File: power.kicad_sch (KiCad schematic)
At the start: 54 parts, among them J2 TYPE-C16PIN, J3 Conn_01x06_Pin, Q5 CSD17575Q3A, Q6 CSD17575Q3A, Q7 CSD17575Q3A, Q8 CSD17575Q3A, U1 FUSB302BMPX, U2 CH224K, U3 BQ25792RQMR, U4 AP2112K-3.3TRG1, U5 AP2112K-1.8TRG1, U6 LP8556SQ-E09/NOPB, U8 ESD7104MUTAG_C2987068, U9 TPS61088RHLR

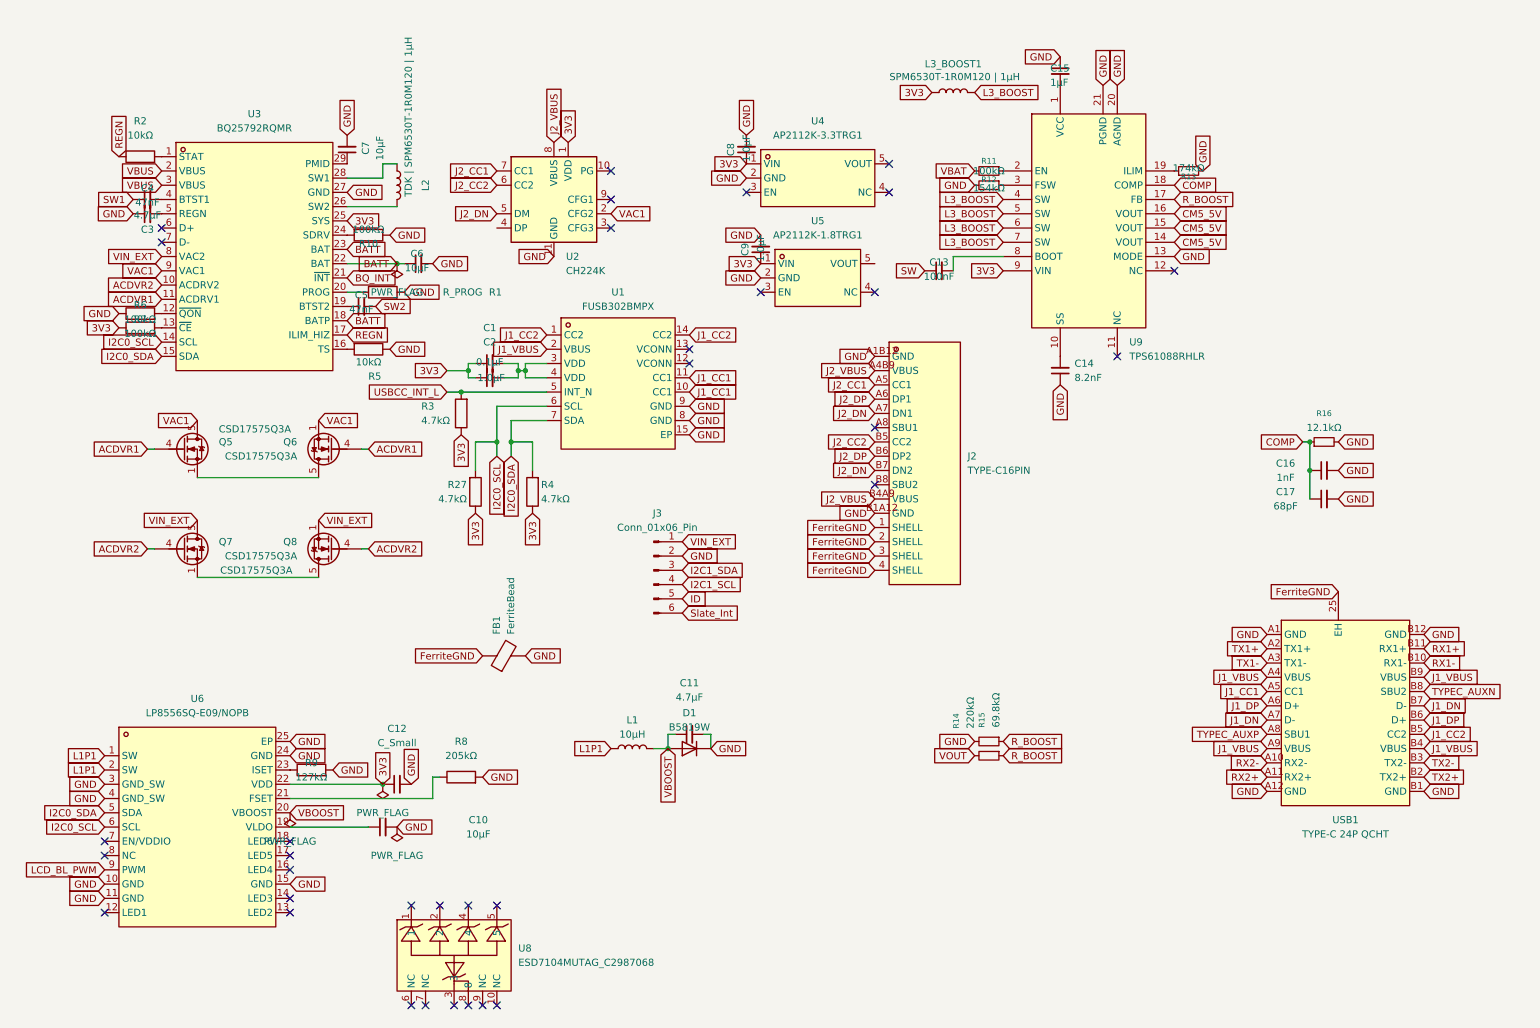
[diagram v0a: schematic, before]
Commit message: Move Data USB-C Port to IO + Add USB1 SS mux and SBU orientation switch, resolve CM5 GPIO assignments
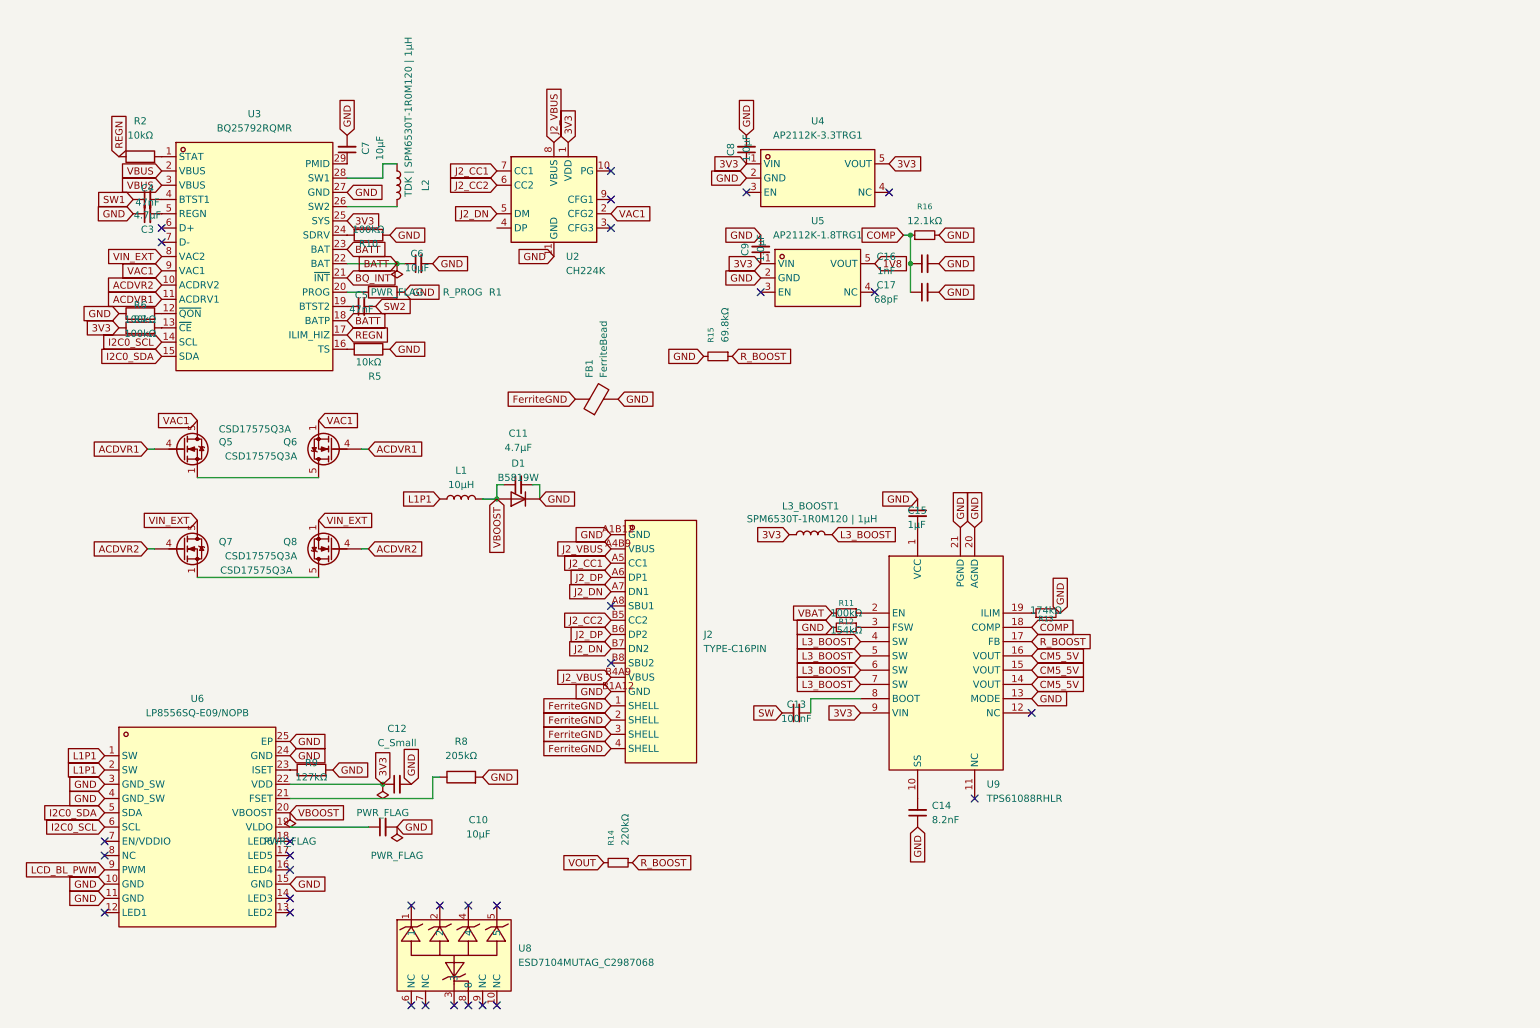
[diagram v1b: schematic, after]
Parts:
- removed C1: 0.1µF, symbol Device:C_Small
- removed C2: 1.0µF, symbol Device:C_Small
- removed J3: Conn_01x06_Pin, symbol Connector:Conn_01x06_Pin
- removed R27, R3, R4: 4.7kΩ, symbol Device:R
- removed U1: FUSB302BMPX, slate113:MLP-14_L2.5-W2.5-P0.50-BL-EP, symbol slate113:FUSB302BMPX
- removed USB1: TYPE-C 24P QCHT, slate113:TYPE-C-SMD_TYPE-C-24P-QCHT, symbol slate113:TYPE-C24PQCHT
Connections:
- net 3V3: now also U4.5 (VOUT)
- net 1V8: now reaches U5.5 (VOUT)
- no-connect marks 34 -> 31
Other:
- moved on the sheet: C11, C13, C14, C15, C16, C17, D1, FB1, J2, L1, L3_BOOST1, R11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

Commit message: add wifi+ble combo symbol, fix connector pin counts, slim b2b connectors, drop 3-way flex cable
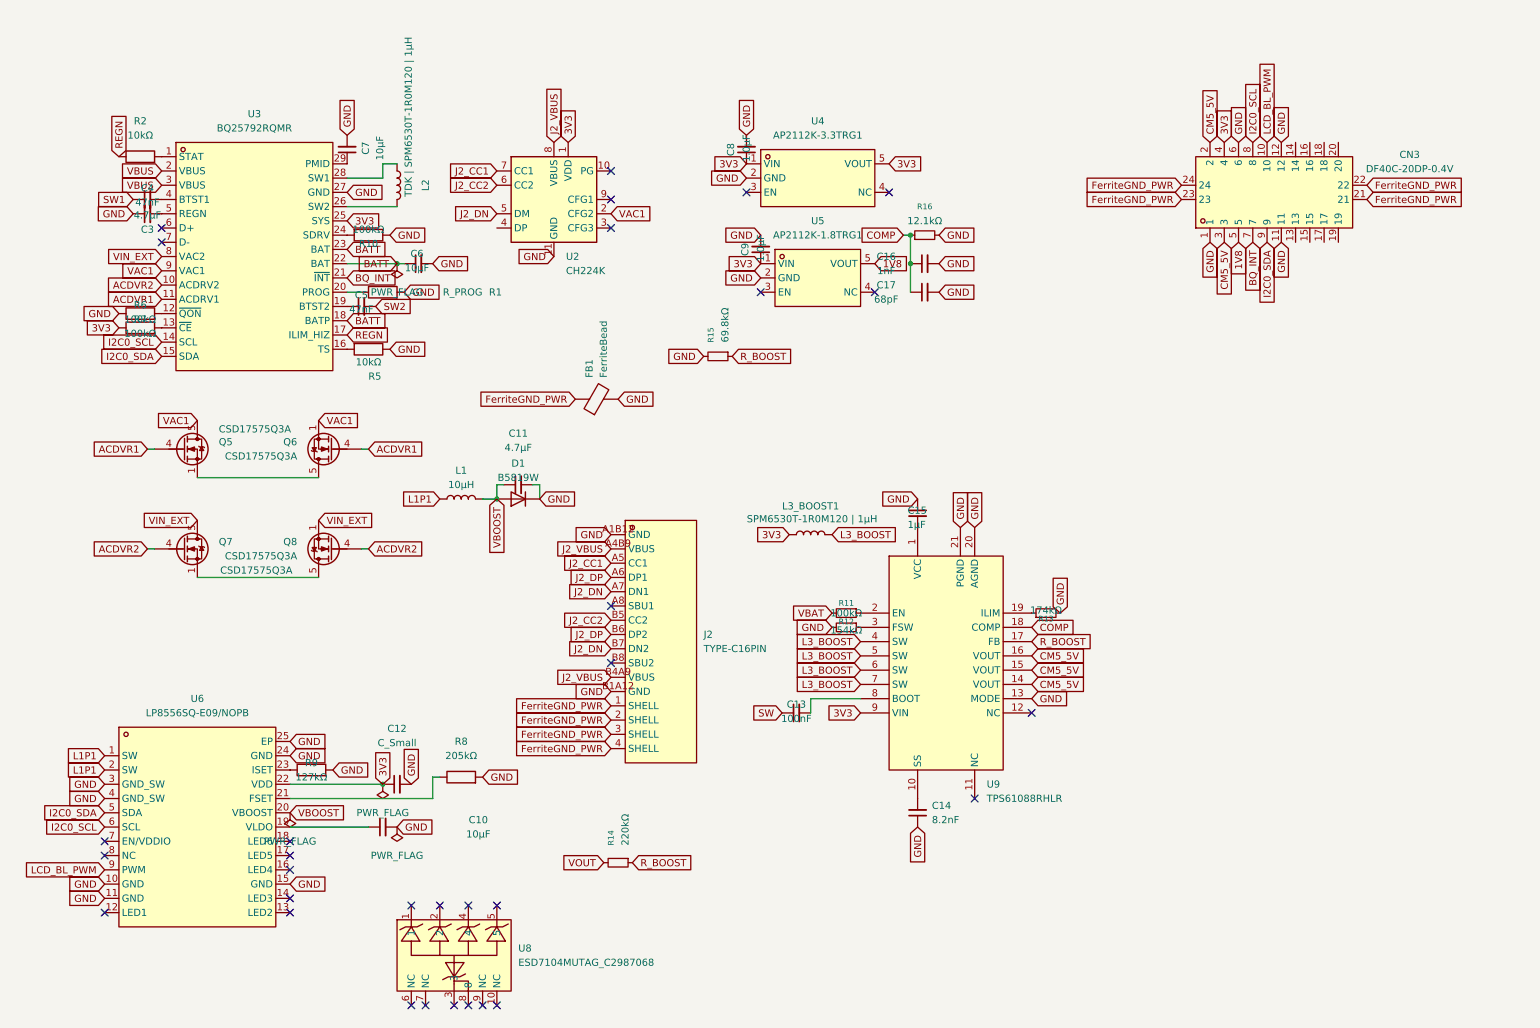
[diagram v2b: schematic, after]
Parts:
- added CN3: DF40C-20DP-0.4V, slate113:CONN-SMD_20P-P0.40_HRS_DF40TC-20DP-0.4V, symbol slate113:DF40C-20DP-0.4V
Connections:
- net 1V8: now also CN3.5
- net 3V3: now also CN3.4
- net BQ_INT: now also CN3.7
- net CM5_5V: now also CN3.2, CN3.3
- net GND: now also CN3.1, CN3.11, CN3.12, CN3.6
- net I2C0_SCL: now also CN3.8
- net I2C0_SDA: now also CN3.9
- net LCD_BL_PWM: now also CN3.10
- net FerriteGND renamed FerriteGND_PWR
- net FerriteGND_PWR: now also CN3.21, CN3.22, CN3.23, CN3.24

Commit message: forgot to save
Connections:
- no-connect marks 31 -> 40
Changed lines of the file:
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@@
 	)
 	(no_connect
+		(at 247.65 52.07)
+	)
+	(no_connect
 		(at 123.19 44.45)
 	)
@@
 	)
 	(no_connect
+		(at 102.87 49.53)
+	)
+	(no_connect
 		(at 66.04 168.91)
 	)
 	(no_connect
+		(at 252.73 34.29)
+	)
+	(no_connect
 		(at 123.19 39.37)
 	)
@@
 	)
 	(no_connect
+		(at 247.65 34.29)
+	)
+	(no_connect
 		(at 43.18 49.53)
 	)
 	(no_connect
+		(at 252.73 52.07)
+	)
+	(no_connect
 		(at 102.87 170.18)
 	)
@@
 	)
 	(no_connect
+		(at 250.19 34.29)
+	)
+	(no_connect
 		(at 187.96 151.13)
 	)
@@
 	)
 	(no_connect
+		(at 245.11 34.29)
+	)
+	(no_connect
 		(at 66.04 171.45)
 	)
@@
 	)
 	(no_connect
+		(at 250.19 52.07)
+	)
+	(no_connect
 		(at 33.02 161.29)
 	)
@@
 	)
 	(no_connect
+		(at 245.11 52.07)
+	)
+	(no_connect
 		(at 100.33 187.96)
 	)
@@
 		(in_pos_files yes)
 		(dnp no)
-		(fields_autoplaced yes)
 		(property "Reference" "#FLG05"
 			(at 66.04 155.575 0)
@@
 		)
 		(property "Value" "PWR_FLAG"
-			(at 66.04 158.75 0)
+			(at 72.898 158.75 0)
 			(show_name no)
 			(do_not_autoplace no)

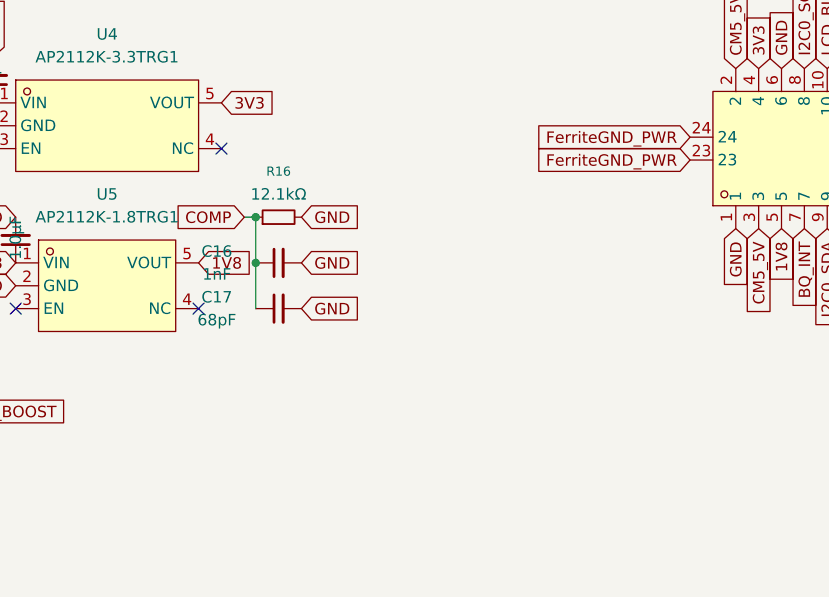
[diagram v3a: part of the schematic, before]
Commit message: finished rf sense and io board closure, added audio system with pcm and three spdt switches, made changes tp lte module, added ldo and sd/sim slot, updated m.2/audio schematics, added new mic msop qfn sot footprints, and added a protection system for non EM06-A Cards
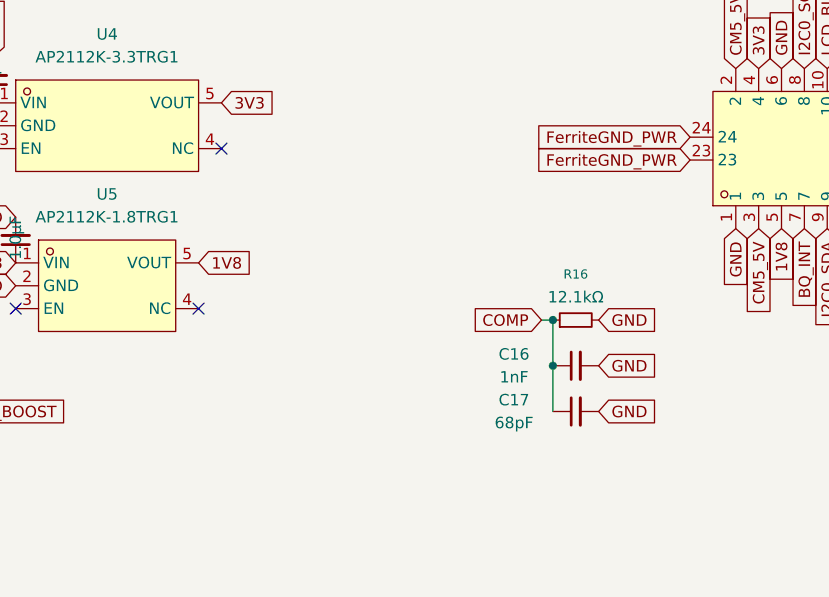
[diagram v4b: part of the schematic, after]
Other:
- moved on the sheet: C16, C17, R16
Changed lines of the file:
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@@
 	)
 	(junction
-		(at 176.53 55.88)
+		(at 209.55 67.31)
 		(diameter 0)
 		(color 0 0 0 0)
 	)
 	(junction
-		(at 176.53 50.8)
+		(at 209.55 62.23)
 		(diameter 0)
 		(color 0 0 0 0)
@@
 	(wire
 		(pts
-			(xy 176.53 50.8) (xy 176.53 55.88)
+			(xy 209.55 62.23) (xy 209.55 67.31)
 		)
 		(stroke
@@
 	(wire
 		(pts
-			(xy 175.26 50.8) (xy 176.53 50.8)
+			(xy 208.28 62.23) (xy 209.55 62.23)
 		)
 		(stroke
@@
 	(wire
 		(pts
-			(xy 176.53 55.88) (xy 176.53 60.96)
+			(xy 209.55 67.31) (xy 209.55 72.39)
 		)
 		(stroke
@@
 	(global_label "COMP"
 		(shape input)
-		(at 175.26 50.8 180)
+		(at 208.28 62.23 180)
 		(fields_autoplaced yes)
 		(effects
@@
 		)
 		(property "Intersheetrefs" "${INTERSHEET_REFS}"
-			(at 166.9529 50.8 0)
+			(at 199.9729 62.23 0)
 			(hide yes)
 			(show_name no)
@@
 	(global_label "GND"
 		(shape input)
-		(at 181.61 60.96 0)
+		(at 214.63 72.39 0)
 		(fields_autoplaced yes)
 		(effects
@@
 		)
 		(property "Intersheetrefs" "${INTERSHEET_REFS}"
-			(at 188.4657 60.96 0)
+			(at 221.4857 72.39 0)
 			(hide yes)
 			(show_name no)
@@
 	(global_label "GND"
 		(shape input)
-		(at 181.61 50.8 0)
+		(at 214.63 62.23 0)
 		(fields_autoplaced yes)
 		(effects
@@
 		)
 		(property "Intersheetrefs" "${INTERSHEET_REFS}"
-			(at 188.4657 50.8 0)
+			(at 221.4857 62.23 0)
 			(hide yes)
 			(show_name no)
@@
 	(global_label "GND"
 		(shape input)
-		(at 181.61 55.88 0)
+		(at 214.63 67.31 0)
 		(fields_autoplaced yes)
 		(effects
@@
 		)
 		(property "Intersheetrefs" "${INTERSHEET_REFS}"
-			(at 188.4657 55.88 0)
+			(at 221.4857 67.31 0)
 			(hide yes)
 			(show_name no)
@@
 	(symbol
 		(lib_id "Device:R_Small")
-		(at 179.07 50.8 90)
+		(at 212.09 62.23 90)
 		(unit 1)
 		(body_style 1)
@@
 		(fields_autoplaced yes)
 		(property "Reference" "R16"
-			(at 179.07 45.72 90)
+			(at 212.09 57.15 90)
 			(show_name no)
 			(do_not_autoplace no)
@@
 		)
 		(property "Value" "12.1kΩ"
-			(at 179.07 48.26 90)
+			(at 212.09 59.69 90)
 			(show_name no)
 			(do_not_autoplace no)
@@
 		)
 		(property "Footprint" ""
-			(at 179.07 50.8 0)
+			(at 212.09 62.23 0)
 			(hide yes)
 			(show_name no)
@@
 		)
 		(property "Datasheet" ""
-			(at 179.07 50.8 0)
+			(at 212.09 62.23 0)
 			(hide yes)
 			(show_name no)
@@
 		)
 		(property "Description" "Resistor, small symbol"
-			(at 179.07 50.8 0)
+			(at 212.09 62.23 0)
 			(hide yes)
 			(show_name no)
@@
 	(symbol
 		(lib_id "Device:C_Small")
-		(at 179.07 60.96 90)
+		(at 212.09 72.39 90)
 		(unit 1)
 		(body_style 1)
@@
 		(dnp no)
 		(property "Reference" "C17"
-			(at 172.212 59.69 90)
+			(at 205.232 71.12 90)
 			(show_name no)
 			(do_not_autoplace no)
@@
 		)
 		(property "Value" "68pF"
-			(at 172.212 62.23 90)
+			(at 205.232 73.66 90)
 			(show_name no)
 			(do_not_autoplace no)
@@
 		)
 		(property "Footprint" ""
-			(at 179.07 60.96 0)
+			(at 212.09 72.39 0)
 			(hide yes)
 			(show_name no)
@@
 		)
 		(property "Datasheet" ""
-			(at 179.07 60.96 0)
+			(at 212.09 72.39 0)
 			(hide yes)
 			(show_name no)
@@
 		)
 		(property "Description" "Unpolarized capacitor, small symbol"
-			(at 179.07 60.96 0)
+			(at 212.09 72.39 0)
 			(hide yes)
 			(show_name no)
@@
 	(symbol
 		(lib_id "Device:C_Small")
-		(at 179.07 55.88 90)
+		(at 212.09 67.31 90)
 		(unit 1)
 		(body_style 1)
@@
 		(dnp no)
 		(property "Reference" "C16"
-			(at 172.212 54.61 90)
+			(at 205.232 66.04 90)
 			(show_name no)
 			(do_not_autoplace no)
@@
 		)
 		(property "Value" "1nF"
-			(at 172.212 57.15 90)
+			(at 205.232 68.58 90)
 			(show_name no)
 			(do_not_autoplace no)
@@
 		)
 		(property "Footprint" ""
-			(at 179.07 55.88 0)
+			(at 212.09 67.31 0)
 			(hide yes)
 			(show_name no)
@@
 		)
 		(property "Datasheet" ""
-			(at 179.07 55.88 0)
+			(at 212.09 67.31 0)
 			(hide yes)
 			(show_name no)
@@
 		)
 		(property "Description" "Unpolarized capacitor, small symbol"
-			(at 179.07 55.88 0)
+			(at 212.09 67.31 0)
 			(hide yes)
 			(show_name no)
